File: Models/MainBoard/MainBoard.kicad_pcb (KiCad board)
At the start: 2 copper layers, 4 parts

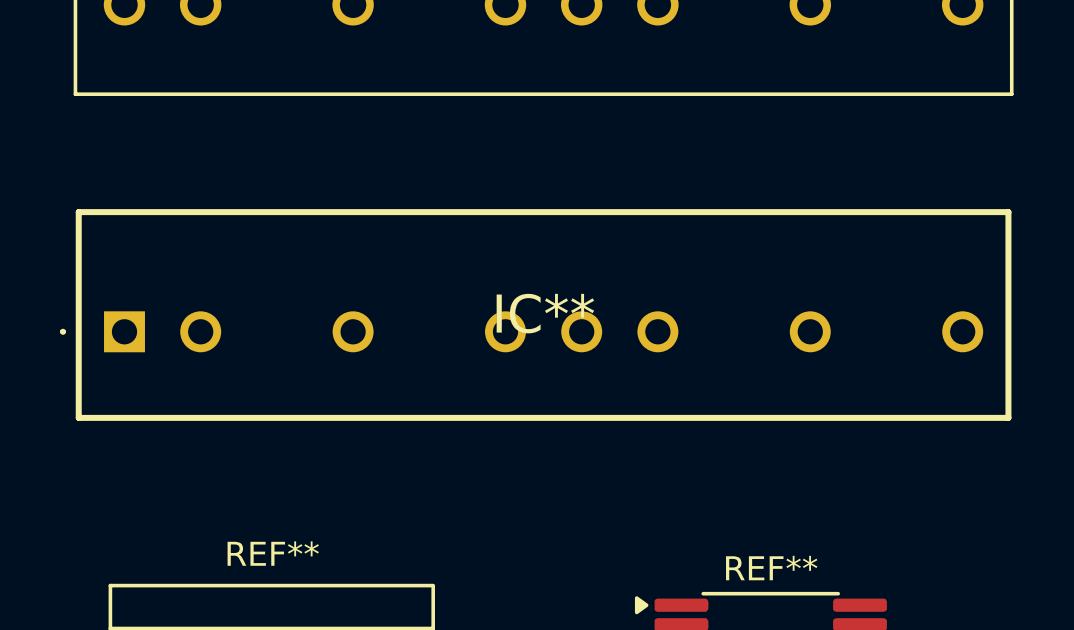
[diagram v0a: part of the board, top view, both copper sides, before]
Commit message: Remove old PA95 footprint from board
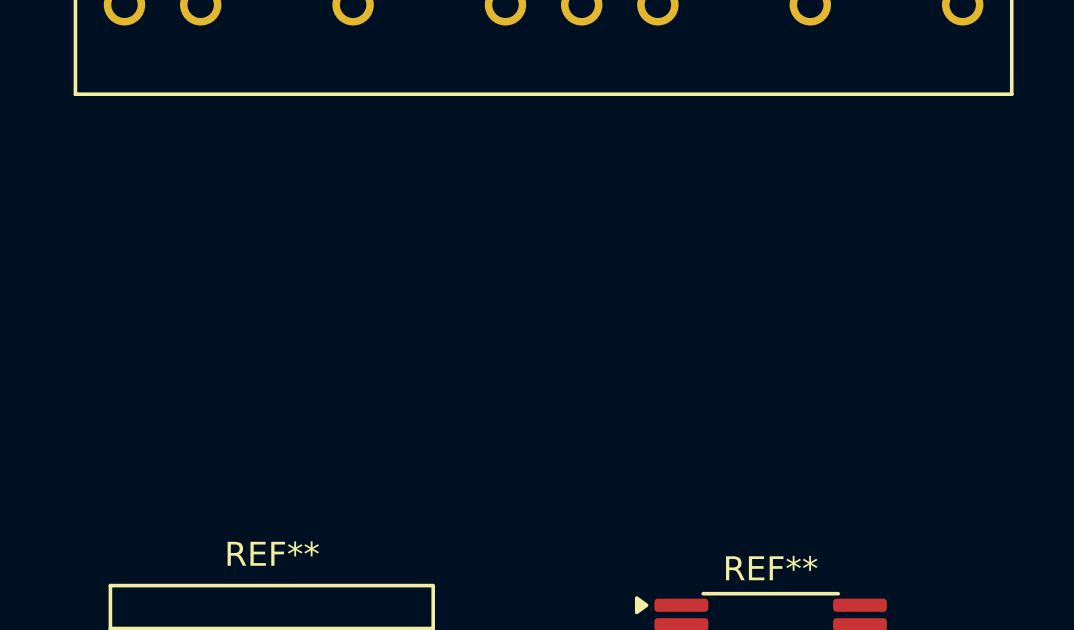
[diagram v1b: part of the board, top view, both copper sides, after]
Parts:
- removed IC**: PA95, PA95:PA95

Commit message: Save progress
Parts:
- added REF**: SOIC-16-Wide, IC:SOIC-16-Wide, F.Cu at (152.2, 111.7)
- added REF**: VQFN-32, IC:VQFN-32, F.Cu at (167.2, 95.2)
- added REF**: SOIC-8, IC:SOIC-8, F.Cu at (135.1, 108.6)
- moved REF** 2.05 mm to (143.3, 74.9)

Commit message: Save progress
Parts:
- removed the REF** at (143.3, 74.9)
- removed the REF** at (151.6, 95.3)
- removed the REF** at (152.2, 111.7)
- removed the REF** at (167.2, 95.2)
- removed the REF** at (135.1, 108.6)
- removed the REF** at (134.9, 95.6)
- added REF**: TSSOP-16, IC:TSSOP-16, F.Cu at (139.1, 96.8)
- added REF**: SOIC-16-Wide, IC:SOIC-16-Wide, F.Cu at (157.1, 112.8)
- added REF**: PinSocket_1x24, Connector_Custom:PinSocket_1x24, F.Cu at (182.9, 88.9)
- added REF**: VQFN-32, IC:VQFN-32, F.Cu at (138.9, 79.8)
- added REF**: TSSOP-16, IC:TSSOP-16, F.Cu at (139.4, 113.3)
- added REF**: PinSocket_1x24, Connector_Custom:PinSocket_1x24, F.Cu at (167.6, 88.9)
- added REF**: SOIC-16-Wide, IC:SOIC-16-Wide, F.Cu at (157.2, 80.0)
- added REF**: VQFN-32, IC:VQFN-32, F.Cu at (139.0, 65.3)
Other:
- board outline added: 54.6 x 62.4 mm
- board text added: "0.1524 mm / 0.1524 mm"
- board text added: "0.2540 mm"
- board text added: "1.6256 mm"
- board text added: "2"
- board text added: "54.6000 mm x 62.4000 mm"
- board text added: "BOARD CHARACTERISTICS"
- board text added: "Board Thickness:"
- board text added: "Board overall dimensions:"
- board text added: "Castellated pads:"
- board text added: "Copper Finish:"
- board text added: "Copper Layer Count:"
- board text added: "Edge card connectors:"
- board text added: "Impedance Control:"
- board text added: "Min hole diameter:"
- board text added: "Min track/spacing:"
- board text added: "No"
- board text added: "None"
- board text added: "Plated Board Edge:"

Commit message: Save progress
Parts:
- removed the REF** at (138.9, 79.8)
- removed the REF** at (139.0, 65.3)
- added REF**: VQFN-32, IC:VQFN-32, F.Cu at (139.4, 79.8)
- added REF**: VQFN-32, IC:VQFN-32, F.Cu at (139.4, 65.2)
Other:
- copper layers 2 -> 4
- board text removed: "0.1524 mm / 0.1524 mm"
- board text removed: "0.2540 mm"
- board text removed: "1.6256 mm"
- board text removed: "2"
- board text removed: "54.6000 mm x 62.4000 mm"
- board text removed: "BOARD CHARACTERISTICS"
- board text removed: "Board Thickness:"
- board text removed: "Board overall dimensions:"
- board text removed: "Castellated pads:"
- board text removed: "Copper Finish:"
- board text removed: "Copper Layer Count:"
- board text removed: "Edge card connectors:"
- board text removed: "Impedance Control:"
- board text removed: "Min hole diameter:"
- board text removed: "Min track/spacing:"
- board text removed: "No"
- board text removed: "None"
- board text removed: "Plated Board Edge:"

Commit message: Save progress
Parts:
- added REF**: DowelPin_2.5mm, Connector_Custom:DowelPin_2.5mm, F.Cu at (153.4, 65.1)
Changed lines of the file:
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@@
 			(outputformat 1)
 			(mirror no)
-			(drillshape 1)
+			(drillshape 0)
 			(scaleselection 1)
-			(outputdirectory "")
+			(outputdirectory "../../../../../Desktop/Gerbers/")
 		)
 	)
@@
 		)
 		(embedded_fonts no)
+	)
+	(footprint "Connector_Custom:DowelPin_2.5mm"
+		(layer "F.Cu")
+		(at 153.4 65.1)
+		(property "Reference" "REF**"
+			(at 0 -9.94 0)
+			(unlocked yes)
+			(layer "F.SilkS")
+			(effects
+				(font
+					(size 0.8 0.8)
+					(thickness 0.12)
+				)
+			)
+		)
+		(property "Value" "DowelPin_2.5mm"
+			(at 0 -8.74 0)
+			(unlocked yes)
+			(layer "F.Fab")
+			(effects
+				(font
+					(size 0.8 0.8)
+					(thickness 0.12)
+				)
+			)
+		)
+		(property "Datasheet" ""
+			(at 0 0 0)
+			(unlocked yes)
+			(layer "F.Fab")
+			(hide yes)
+			(effects
+				(font
+					(size 0.8 0.8)
+					(thickness 0.12)
+				)
+			)
+		)
+		(property "Description" ""
+			(at 0 0 0)
+			(unlocked yes)
+			(layer "F.Fab")
+			(hide yes)
+			(effects
+				(font
+					(size 0.8 0.8)
+					(thickness 0.12)
+				)
+			)
+		)
+		(attr through_hole)
+		(fp_text user "${REFERENCE}"
+			(at 0 -7.54 0)
+			(unlocked yes)
+			(layer "F.Fab")
+			(effects
+				(font
+					(size 0.8 0.8)
+					(thickness 0.12)
+				)
+			)
+		)
+		(pad "" np_thru_hole circle
+			(at 0 0)
+			(size 2.6 2.6)
+			(drill 2.6)
+			(layers "*.Cu" "*.Paste" "*.Mask")
+		)
+		(embedded_fonts no)

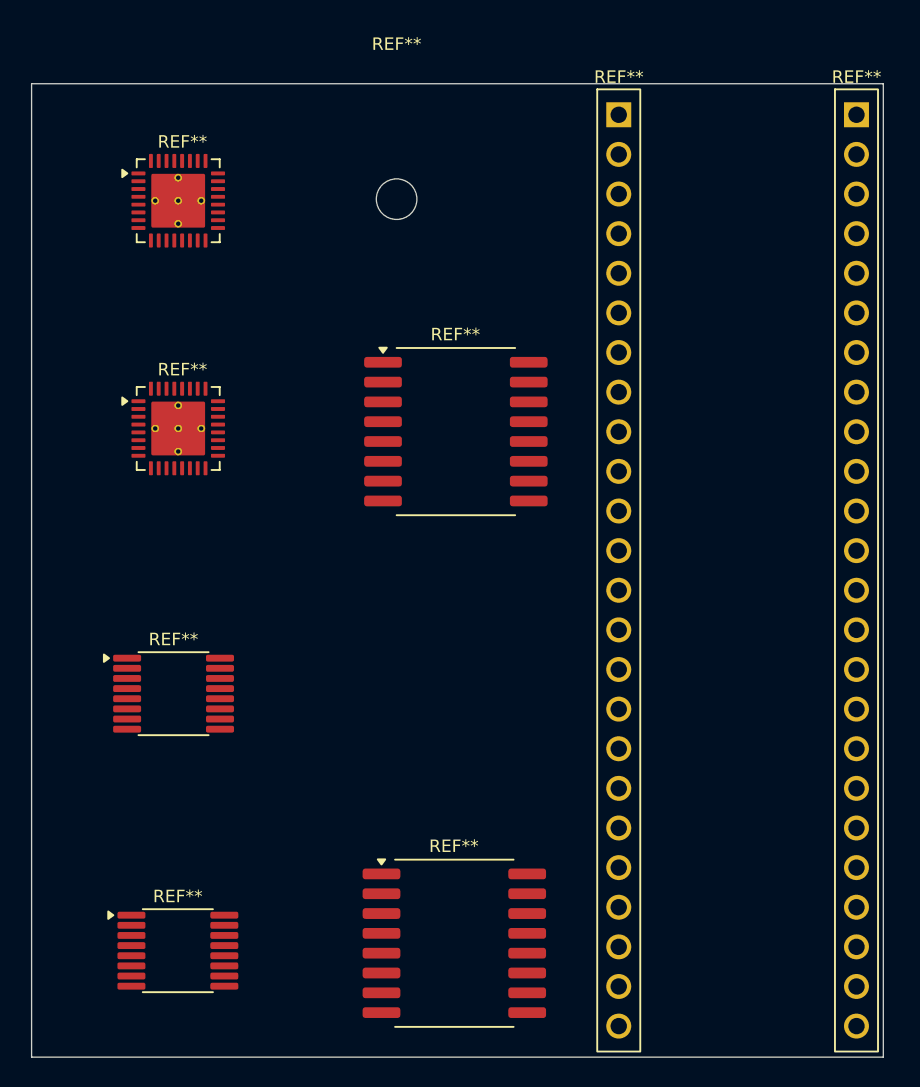
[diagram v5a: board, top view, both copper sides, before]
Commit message: Preparing to revert this change to the footprints
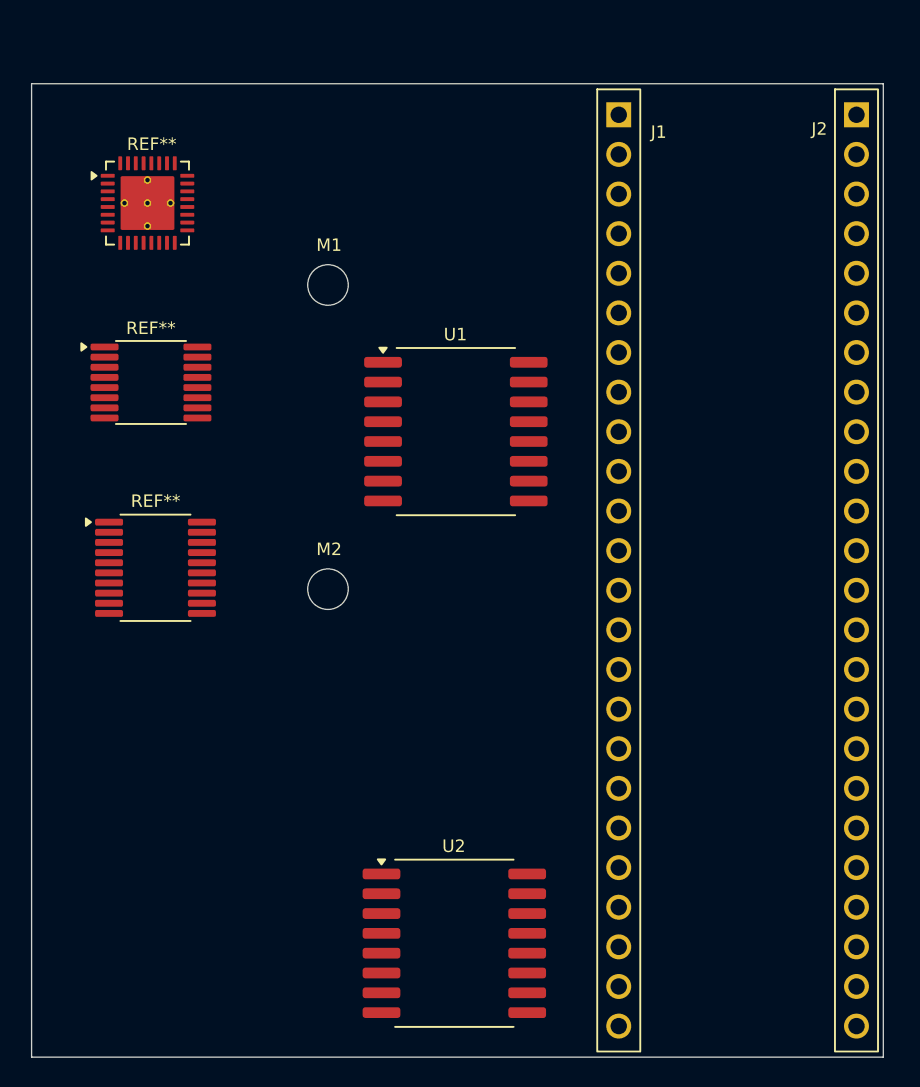
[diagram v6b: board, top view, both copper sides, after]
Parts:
- removed the REF** at (139.1, 96.8)
- removed the REF** at (139.4, 113.3)
- removed the REF** at (153.4, 65.1)
- removed the REF** at (139.4, 79.8)
- removed the REF** at (139.4, 65.2)
- added M1: DowelPin_2.5mm, Connector_Custom:DowelPin_2.5mm, F.Cu at (149.0, 70.6)
- added M2: DowelPin_2.5mm, Connector_Custom:DowelPin_2.5mm, F.Cu at (149.0, 90.1)
- added REF**: VQFN-32, IC:VQFN-32, F.Cu at (137.4, 65.3)
- added REF**: TSSOP-16, IC:TSSOP-16, F.Cu at (137.7, 76.8)
- added REF**: TSSOP-20, IC:TSSOP-20, F.Cu at (137.9, 88.7)
- renumbered REF** to J1, REF** to J2, REF** to U1, REF** to U2

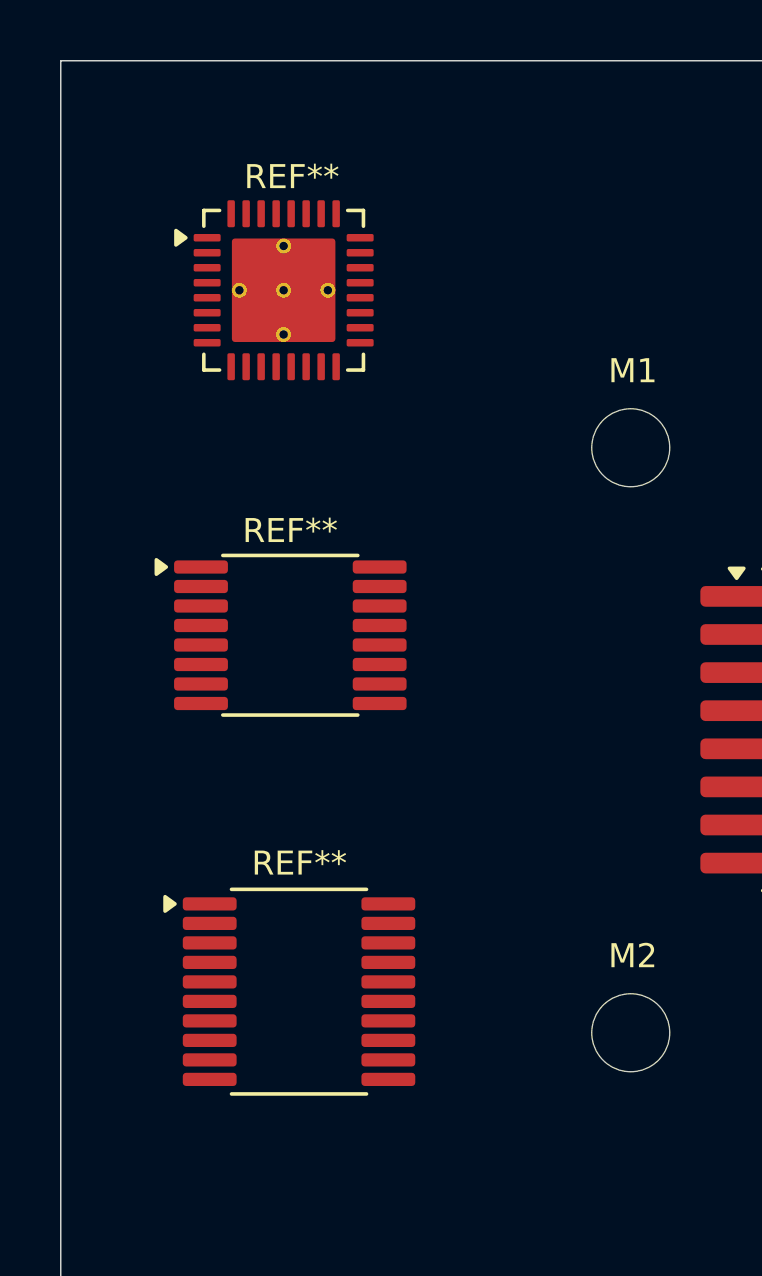
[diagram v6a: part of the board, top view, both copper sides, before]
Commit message: Footprint change has been reverted
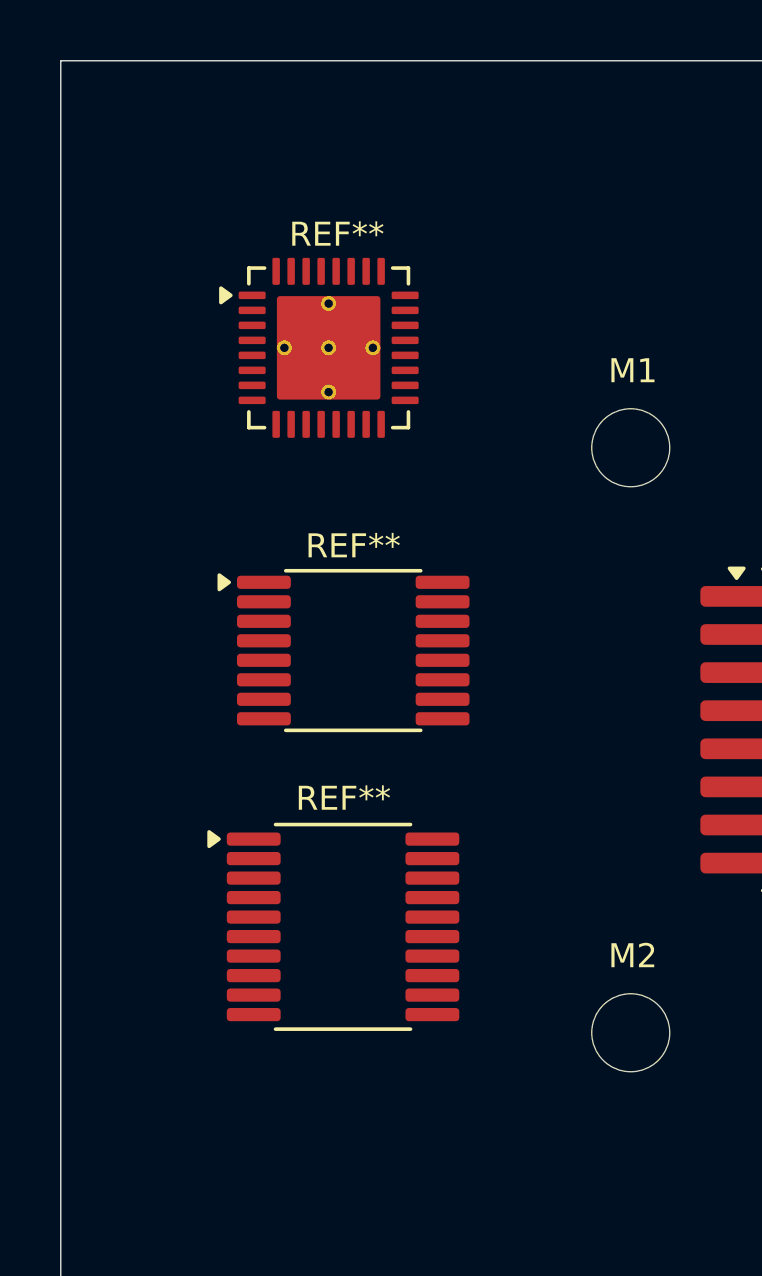
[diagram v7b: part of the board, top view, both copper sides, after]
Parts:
- moved REF** 2.61 mm to (139.4, 86.6)
- moved REF** 2.44 mm to (138.9, 67.3)
- moved REF** 2.16 mm to (139.8, 77.4)
